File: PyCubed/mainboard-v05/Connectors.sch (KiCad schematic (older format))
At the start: 23 parts, among them J1 503182-1852, J11 874370343, J13 USB_C_pycubed, J16 1985807, J17 1985807, J18 1985807, J19 874370343, J2 Conn_01x05, J20 874370343, J21 874370343, J22 874370343, J23 874370343, J24 MOLEX_Sherlock_2pos, J3 MOLEX_Sherlock_2pos, U8 MR25H40MDF

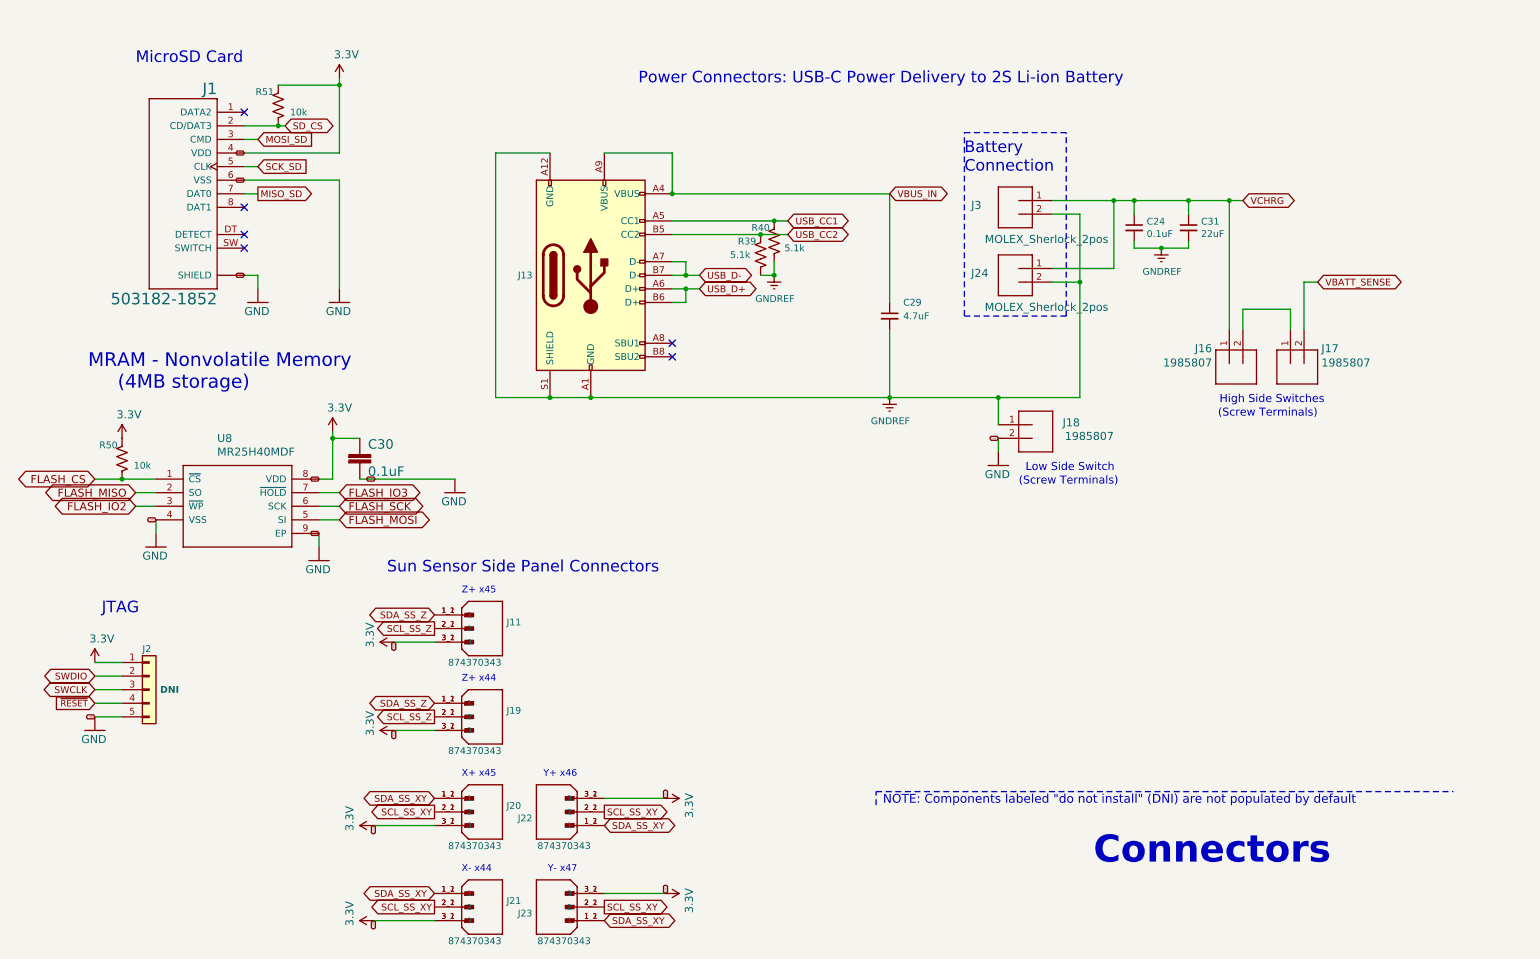
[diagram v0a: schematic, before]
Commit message: Battery board and side panels ready for CAD check and review, pycubed not finished yet
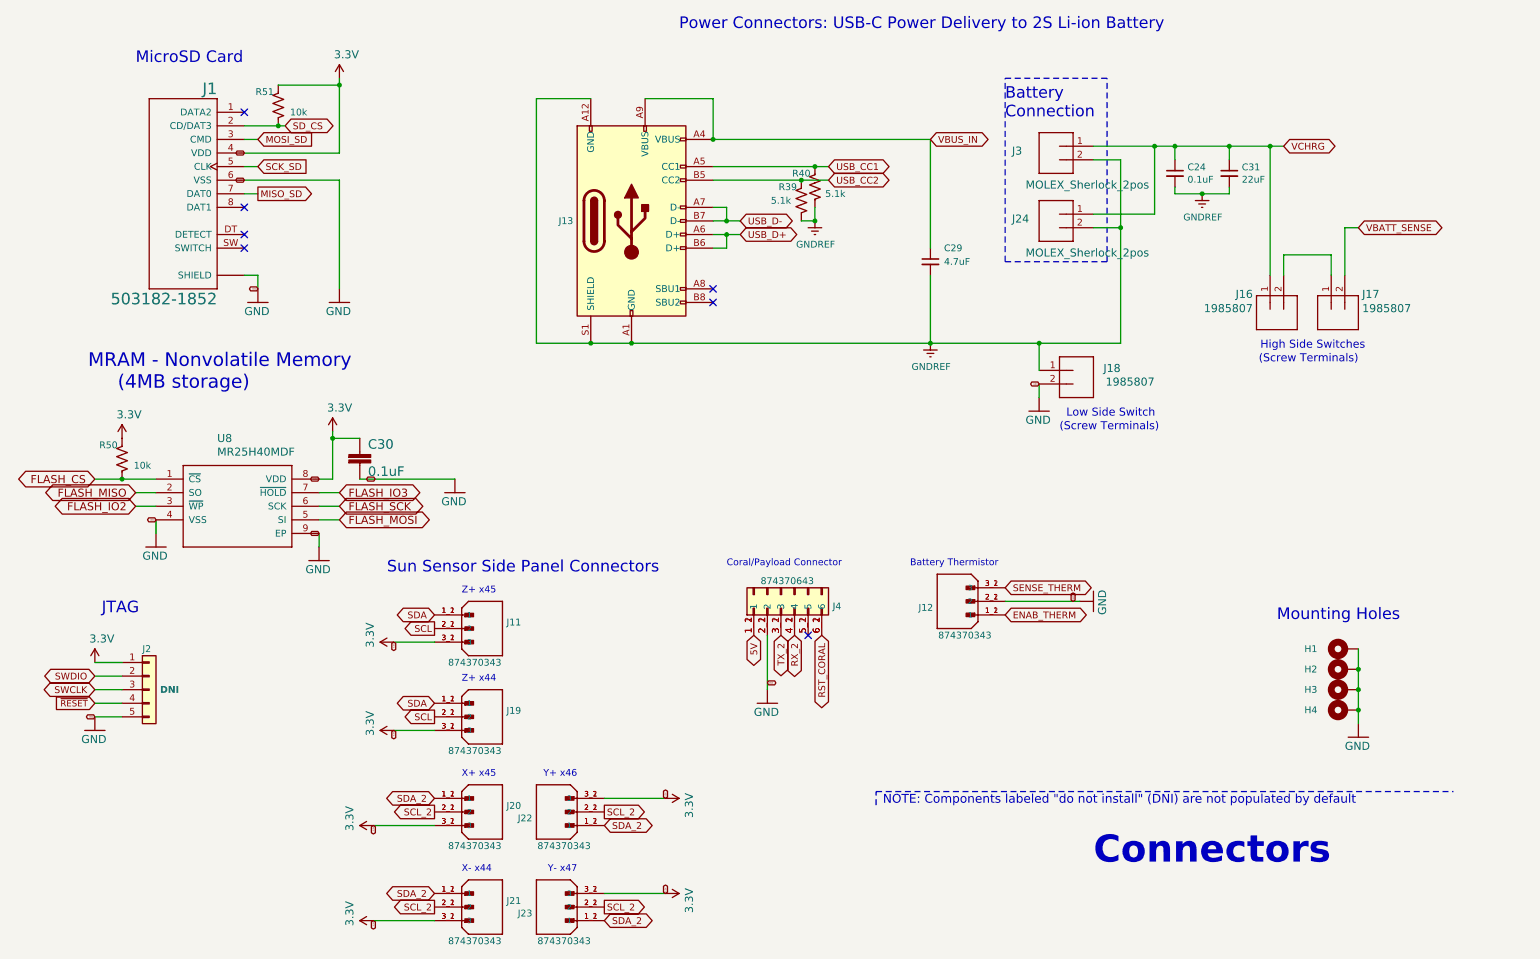
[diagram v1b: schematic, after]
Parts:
- added H1, H2, H3, H4: MountingHole_Pad, MountingHole:MountingHole_3.2mm_M3_DIN965_Pad, symbol Mechanical:MountingHole_Pad
- added J12: 874370343, mainboard:MOLEX_874370343, symbol mainboard:874370343
- added J4: 874370643, mainboard:MOLEX_874370643, symbol mainboard:874370643
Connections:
- net GND: now also J12.2_1 (2), J12.2_2 (2), J4.2_1 (2), J4.2_2 (2)
- net SCL_SS_XY renamed SCL_2
- net SCL_SS_Z renamed SCL
- net SDA_SS_XY renamed SDA_2
- net SDA_SS_Z renamed SDA
- new net: J4.5_1 (5), J4.5_2 (5)
- new net: H1.1, H2.1, H3.1, H4.1
- new net 5V: J4.1_1 (1), J4.1_2 (1)
- new net ENAB_THERM: J12.1_1 (1), J12.1_2 (1)
- new net RST_CORAL: J4.6_1 (6), J4.6_2 (6)
- new net RX_2: J4.4_1 (4), J4.4_2 (4)
- new net SENSE_THERM: J12.3_1 (3), J12.3_2 (3)
- new net TX_2: J4.3_1 (3), J4.3_2 (3)
- no-connect marks 6 -> 7
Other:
- note added: "Battery Thermistor"
- note added: "Coral/Payload Connector"
- note added: "Mounting Holes"
- moved on the sheet: C24, C29, C31, J13, J16, J17, J18, J24, J3, R39, R40

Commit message: pycubed finished, awaiting review
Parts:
- removed J11, J12, J19, J20, J21, J22, J23: 874370343, mainboard:MOLEX_874370343, symbol mainboard:874370343
- removed J17: 1985807, mainboard:SCREWTERMINAL-3.5MM-2_LOCK, symbol mainboard:M023.5MM_LOCK
- removed J24, J3: MOLEX_Sherlock_2pos, mainboard:MOLEX_Sherlock_2pos, symbol mainboard:M023.5MM_LOCK
- removed J4: 874370643, mainboard:MOLEX_874370643, symbol mainboard:874370643
- added J11, J19, J20, J21, J22, J23, J3, J4: 35362-0650, mainboard:MOLEX_35362-0650, symbol mainboard:35362-0650
- added J8, J9: 1985807, mainboard:SCREWTERMINAL-3.5MM-2_LOCK, symbol mainboard:M023.5MM_LOCK
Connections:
- net 3.3V: now also J11.4, J19.4, J20.4, J21.4, J22.4, J23.4
- net 5V: now also J4.1
- net ENAB_THERM: now also J3.6
- net GND: now also J11.3, J19.3, J19.5, J20.3, J20.5, J21.3, J21.5, J22.3, J22.5, J23.3, J23.5, J4.2, J4.5, J8.2
- net GNDREF: now also J3.2, J3.4, J8.1
- net RST_CORAL: now also J4.6
- net RX_2: now also J4.4
- net SCL: now also J11.2, J19.1
- net SCL_2: now also J20.1, J21.1, J22.1, J23.1
- net SDA: now also J11.1, J19.2
- net SDA_2: now also J20.2, J21.2, J22.2, J23.2
- net SENSE_THERM: now also J3.5
- net TX_2: now also J4.3
- net VBATT_SENSE: now also J16.2, J9.2
- net VCHRG: now also J3.1, J3.3, J9.1
- new net BURN: J11.6
- new net VSOLAR: J11.5, J19.6, J20.6, J21.6, J22.6, J23.6
- no-connect marks 7 -> 6
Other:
- note added: "Battery Board"
- note added: "Google Coral"
- note added: "High Side Switches\n(Screw Terminals)"
- note added: "Z- x44"
- note removed: "Battery Thermistor"
- note removed: "High Side Switches"
- note removed: "Z+ x44"
- moved on the sheet: J18
